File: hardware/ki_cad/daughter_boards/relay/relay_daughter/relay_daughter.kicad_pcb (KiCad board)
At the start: 2 copper layers, 42 x 26 mm, 6 parts, among them J1 ToMainPCB, K1 SANYOU_SRD_Form_A, K2 SANYOU_SRD_Form_A

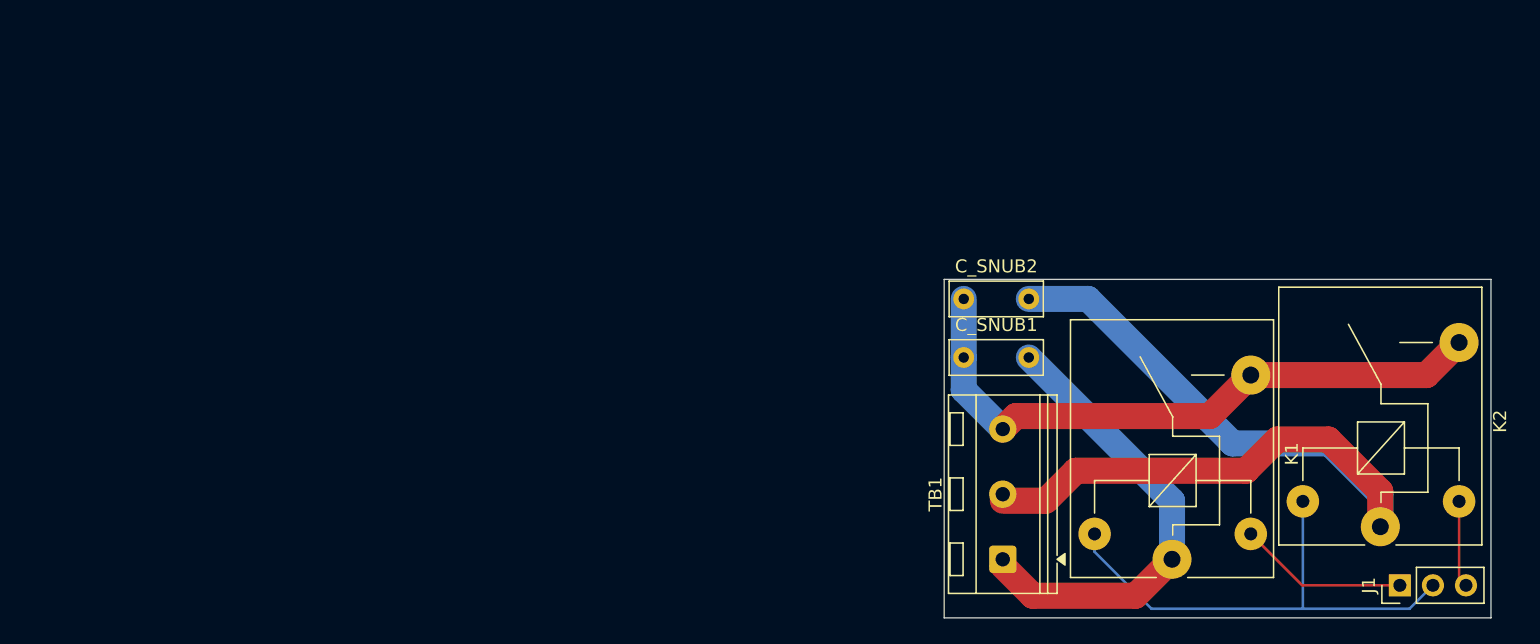
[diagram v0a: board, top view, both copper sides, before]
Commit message: relay daughter PCB frozen, Unisync story frozen
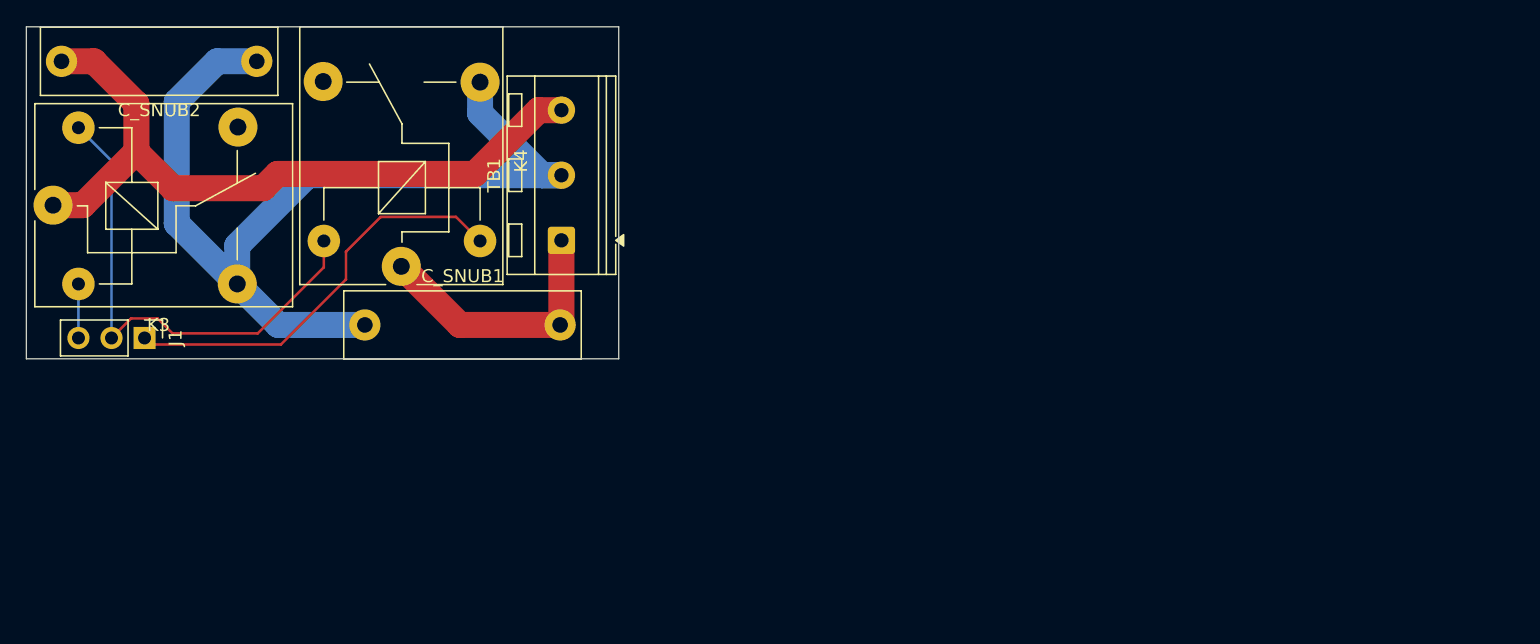
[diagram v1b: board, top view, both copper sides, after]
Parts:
- removed K1, K2: SANYOU_SRD_Form_A, Relay_THT:Relay_SPST_SANYOU_SRD_Series_Form_A
- added K3: SANYOU_SRD_Form_C, Relay_THT:Relay_SPDT_SANYOU_SRD_Series_Form_C, F.Cu at (31.6, 43.8)
- added K4: SANYOU_SRD_Form_C, Relay_THT:Relay_SPDT_SANYOU_SRD_Series_Form_C, F.Cu at (58.3, 48.5)
- added logo1: LOGO, Unisync:Unisync_15mm, B.Cu at (52.5, 40.5)
- C_SNUB1, C_SNUB2: footprint Capacitor_THT:C_Disc_D7.0mm_W2.5mm_P5.00mm -> Capacitor_THT:C_Rect_L18.0mm_W5.0mm_P15.00mm_FKS3_FKP3
- moved J1 98.3 mm to (38.6, 54.0), turned to -90 degrees
- moved C_SNUB2 57.3 mm to (47.2, 32.8), turned to 180 degrees
- moved C_SNUB1 46.1 mm to (55.5, 53.0)
- moved TB1 41.8 mm to (70.6, 46.5)
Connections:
- TB1 pad 2: /LOAD_OUT2 -> /MAINS_LIVE_IN1
- TB1 pad 3: /MAINS_LIVE_IN1 -> /LOAD_OUT2
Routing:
- net /MAINS_LIVE_IN1: track 49.5 -> 75.2 mm
- net /RELAY_OUT1: track 13.1 -> 32.0 mm
- net /LOAD_OUT2: track 71.0 -> 55.2 mm
- net /LOAD_OUT1: track 35.2 -> 20.6 mm
- net /RELAY_OUT2: track 6.67 -> 4.15 mm
- net +5V: track 38.2 -> 38.7 mm
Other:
- board size 42 x 26 mm -> 45.5 x 25.5 mm
